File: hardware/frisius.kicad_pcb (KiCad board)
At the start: 4 copper layers, 50 x 50 mm, 93 parts, among them J1 MEM2067, J2 USB_C_Receptacle_USB2.0, J3 BATTERY, J4 Display, Q1 Q_Dual_NMOS_G1S2G2D2S1D1, SW1 RESET, SW2 BOOT, SW3 POWER, U2 FXOS8700CQR1, U3 MS5637-02BA03, U4 L96-M33, U6 ESP32-S3-WROOM-1, U7 TLV62569DBV, U8 MP2723, U9 MAX17048G

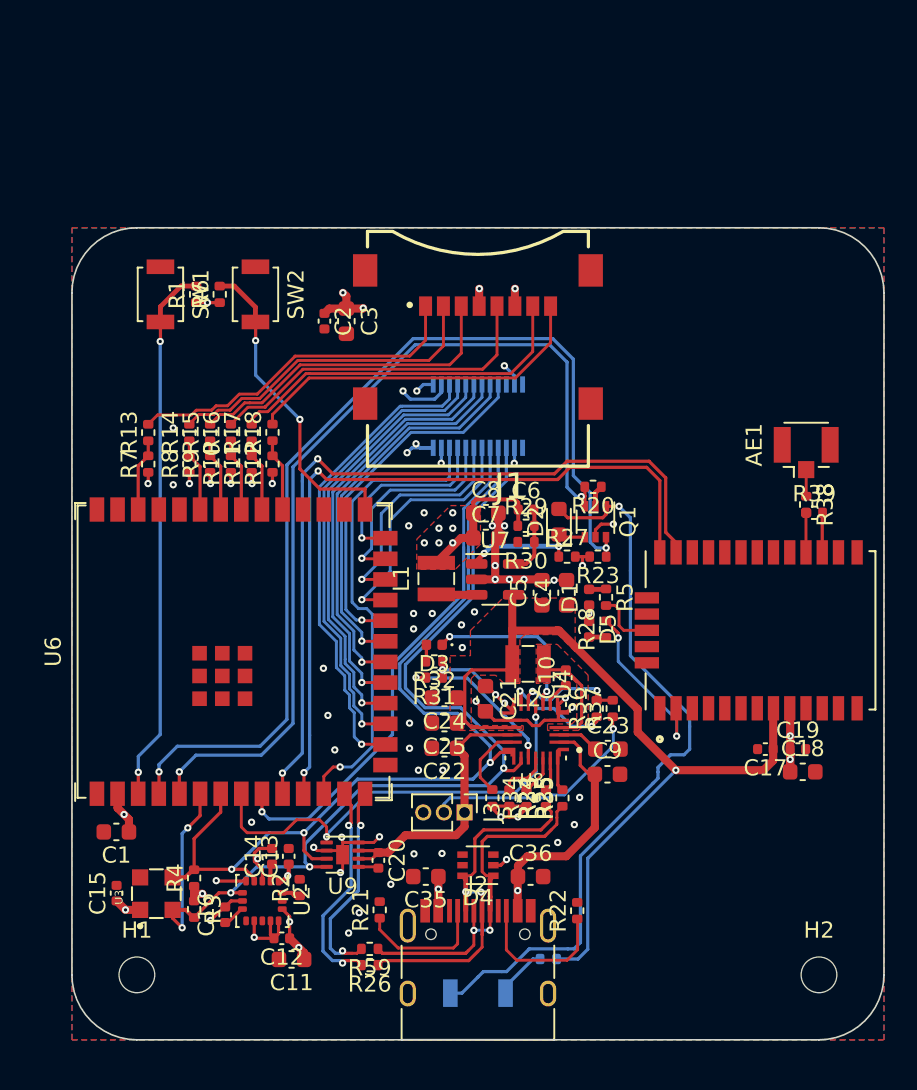
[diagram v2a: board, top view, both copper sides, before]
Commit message: merged in lcdboard test work
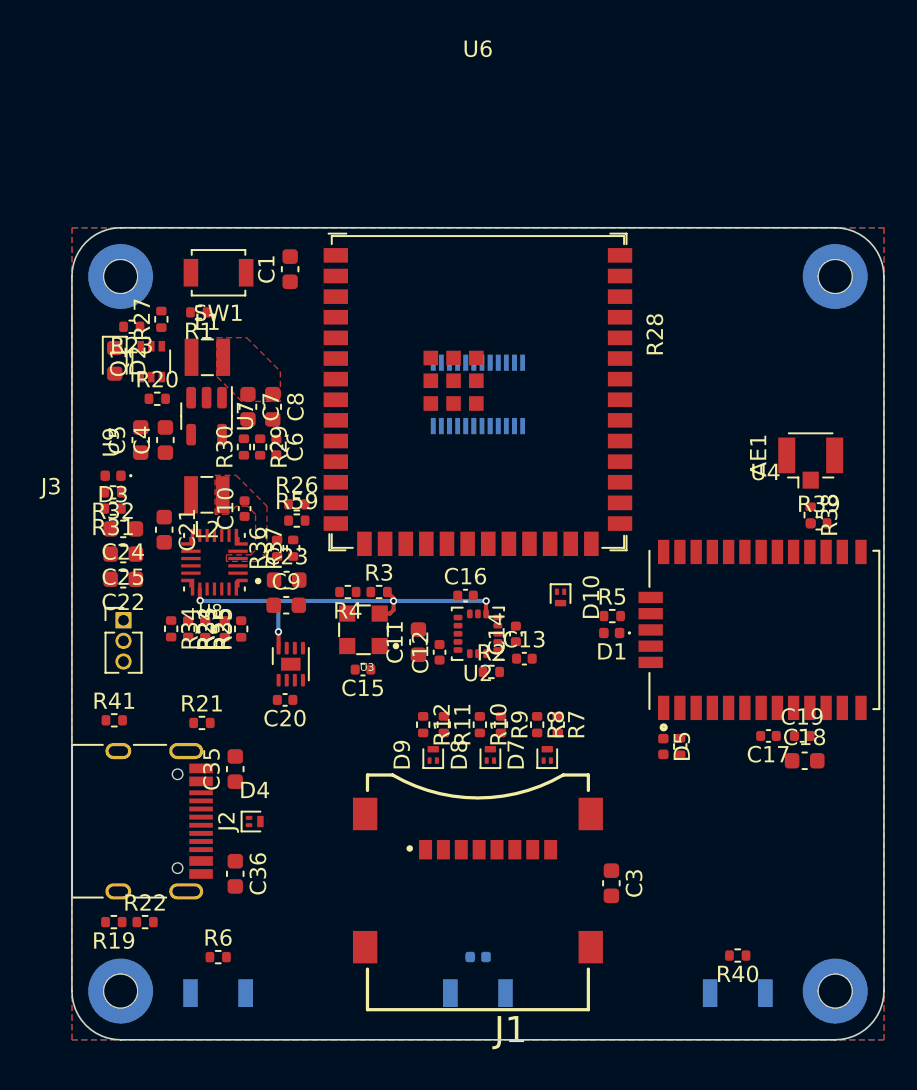
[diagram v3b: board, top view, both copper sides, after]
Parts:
- removed C2: 0.1u, Capacitor_SMD:C_0402_1005Metric
- removed R13, R14, R15, R16, R17, R18: 22, Resistor_SMD:R_0402_1005Metric
- added D10: PESD3V3L2UM, Package_TO_SOT_SMD:SOT-883, F.Cu at (76.7, 106.2)
- added D6: LED_Small_Filled, LED_SMD:LED_0402_1005Metric, B.Cu at (71.6, 128.3)
- added D7: PESD3V3L2UM, Package_TO_SOT_SMD:SOT-883, F.Cu at (75.8, 115.9)
- added D8: PESD3V3L2UM, Package_TO_SOT_SMD:SOT-883, F.Cu at (72.3, 115.9)
- added D9: PESD3V3L2UM, Package_TO_SOT_SMD:SOT-883, F.Cu at (68.8, 115.9)
- added H3: TL, Mounting_Wuerth:Mounting_Wuerth_WA-SMSI-M1.6_H2mm_9774020633, B.Cu at (93.6, 86.5)
- added H4: TR, Mounting_Wuerth:Mounting_Wuerth_WA-SMSI-M1.6_H2mm_9774020633, B.Cu at (49.6, 86.5)
- added R40: R_Small, Resistor_SMD:R_0402_1005Metric, F.Cu at (87.6, 128.3)
- added R41: 1k, Resistor_SMD:R_0402_1005Metric, F.Cu at (49.2, 113.8)
- added SW4: NAV, Button_Switch_SMD:SW_SPST_B3U-1000P, B.Cu at (55.6, 130.6)
- D4: value ESD5V5U5ULCE6327HTSA1 -> PESD3V3L2UM; footprint Package_TO_SOT_SMD:SOT-363_SC-70-6 -> Package_TO_SOT_SMD:SOT-883
- H1, H2: footprint MountingHole:MountingHole_2.2mm_M2_ISO7380 -> Mounting_Wuerth:Mounting_Wuerth_WA-SMSI-M1.6_H2mm_9774020633; moved to B.Cu
- R19: moved to F.Cu
- SW2: moved to B.Cu
- moved SW2 52.3 mm to (87.6, 130.6), turned to 180 degrees
- moved H1 43.0 mm to (93.6, 130.4), turned to 180 degrees
- moved H2 43.0 mm to (49.6, 130.4), turned to 180 degrees
- moved R6 40.8 mm to (55.6, 128.4), turned to 0 degrees
- moved C3 38.3 mm to (79.8, 123.8)
- moved C1 36.3 mm to (60.0, 86.0), turned to 90 degrees
- moved J1 33.5 mm to (71.6, 124.4)
- moved R23 32.0 mm to (50.2, 89.5)
- moved R7 29.9 mm to (76.5, 114.0), turned to -90 degrees
- moved D2 29.1 mm to (49.2, 91.6), turned to -90 degrees
- moved Q1 29.1 mm to (51.5, 91.7), turned to 90 degrees
- moved R27 28.9 mm to (52.1, 89.1), turned to 90 degrees
- moved R26 28.7 mm to (60.4, 100.5), turned to 0 degrees
- moved R20 27.4 mm to (51.8, 94.0), turned to 0 degrees
- moved R19 26.9 mm to (49.1, 126.2), turned to 180 degrees
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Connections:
- D4 pad 2: GND -> /Power/PORT_D-
- D4 pad 3: unconnected-(D4-Pad3) -> GND
- J1 pad 1: Net-(J1-Pad1) -> /Processor/SDMMC.D2
- J1 pad 2: Net-(J1-Pad2) -> /Processor/SDMMC.D3
- J1 pad 3: Net-(J1-Pad3) -> /Processor/SDMMC.CMD
- J1 pad 5: Net-(J1-Pad5) -> /Processor/SDMMC.CLK
- J1 pad 7: Net-(J1-Pad7) -> /Processor/SDMMC.D0
- J1 pad 8: Net-(J1-Pad8) -> /Processor/SDMMC.D1
- J4 pad 10: /Display/TOUCH_INT -> /Display/SYS_I2C.SCL
- J4 pad 12: /Display/MUXLINE0 -> /Display/LCD_SPI_CTRL
- J4 pad 14: /Display/MUXLINE1 -> /Display/MUXLINE3
- J4 pad 18: /Display/MUXLINE3 -> /Display/MUXLINE1
- J4 pad 20: /Display/LCD_SPI_CTRL -> /Display/MUXLINE0
- J4 pad 6: /Display/SYS_I2C.SDA -> /Display/TOUCH_INT
- J4 pad 8: /Display/SYS_I2C.SCL -> /Display/SYS_I2C.SDA
- R10 pad 2: /Processor/SDMMC.CLK -> /Processor/SDMMC.CMD
- R11 pad 2: /Processor/SDMMC.D0 -> /Processor/SDMMC.D3
- R12 pad 2: /Processor/SDMMC.D1 -> /Processor/SDMMC.D2
- R7 pad 2: /Processor/SDMMC.D2 -> /Processor/SDMMC.D1
- R8 pad 2: /Processor/SDMMC.D3 -> /Processor/SDMMC.D0
- R9 pad 2: /Processor/SDMMC.CMD -> /Processor/SDMMC.CLK
- U6 pad 10: /GPS/GPS_UART.RX -> unconnected-(U6-Pad10)
- U6 pad 11: /GPS/GPS_UART.TX -> unconnected-(U6-Pad11)
- U6 pad 12: /Display/LCD_SPI_CTRL -> unconnected-(U6-Pad12)
- U6 pad 15: /Processor/STATUS_LED -> Net-(R41-Pad2)
- U6 pad 16: /Display/DISPLAY_BL -> unconnected-(U6-Pad16)
- U6 pad 17: /Display/RGB.R0 -> /Display/MUXLINE0
- U6 pad 18: /Display/RGB.R1 -> /Display/MUXLINE1
- U6 pad 19: /Display/RGB.G0 -> /Display/MUXLINE2
- U6 pad 20: /Display/RGB.G1 -> /Display/MUXLINE3
- U6 pad 21: /Display/RGB.B0 -> /Display/LCD_SPI_CTRL
- U6 pad 22: /Display/RGB.B1 -> /Power/POWER_BUTTON
- U6 pad 23: /Display/MUXLINE0 -> /Power/SHUTDOWN
- U6 pad 24: /Display/MUXLINE1 -> /Display/SYS_I2C.SCL
- U6 pad 25: /Display/MUXLINE2 -> /Display/SYS_I2C.SDA
- U6 pad 26: /Display/MUXLINE3 -> /Display/TOUCH_INT
- U6 pad 31: /Processor/SDMMC.D1 -> /Display/RGB.B1
- U6 pad 32: /Processor/SDMMC.D0 -> /Display/RGB.B0
- U6 pad 33: /Processor/SDMMC.CLK -> /Display/RGB.G1
- U6 pad 34: /Processor/SDMMC.CMD -> /Display/RGB.G0
- U6 pad 35: /Processor/SDMMC.D3 -> /Display/RGB.R1
- U6 pad 38: /Processor/SDMMC.D2 -> /Display/RGB.R0
- U6 pad 4: /Power/POWER_BUTTON -> unconnected-(U6-Pad4)
- U6 pad 5: /Power/SHUTDOWN -> unconnected-(U6-Pad5)
- U6 pad 6: /Display/SYS_I2C.SDA -> unconnected-(U6-Pad6)
- U6 pad 7: /Display/SYS_I2C.SCL -> unconnected-(U6-Pad7)
- U6 pad 8: /Power/BMS_INT -> unconnected-(U6-Pad8)
- U6 pad 9: /Display/TOUCH_INT -> unconnected-(U6-Pad9)
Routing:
- net /Power/POWER_BUTTON: track 61.9 -> 0.00 mm, vias 2 -> 0
- net /Display/SYS_I2C.SCL: track 59.4 -> 0.00 mm, vias 3 -> 0
- net /Power/SHUTDOWN: track 56.1 -> 0.00 mm, vias 2 -> 0
- net GND: track 53.6 -> 0.00 mm, vias 53 -> 0
- net VDD_NVDC: track 52.7 -> 0.00 mm, vias 1 -> 0
- net /GPS/GPS_UART.RX: track 48.9 -> 0.00 mm, vias 2 -> 0
- net /GPS/GPS_UART.TX: track 46.6 -> 0.00 mm, vias 2 -> 0
- net Net-(D2-Pad2): track 45.7 -> 0.00 mm, vias 1 -> 0
- net +3V3: track 44.5 -> 0.00 mm, vias 29 -> 0
- net /Display/SYS_I2C.SDA: track 65.2 -> 24.3 mm, vias 5 -> 4
- net /Processor/RST_BTN: track 33.3 -> 0.00 mm, vias 2 -> 0
- net /Display/TOUCH_INT: track 31.6 -> 0.00 mm, vias 1 -> 0
- net /Display/DISPLAY_BL: track 29.5 -> 0.00 mm, vias 1 -> 0
- net /Display/LCD_SPI_CTRL: track 29.1 -> 0.00 mm, vias 1 -> 0
- net /Display/RGB.R0: track 28.3 -> 0.00 mm, vias 1 -> 0
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- removed copper zone on F.Cu, net VDD_NVDC
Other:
- outline, holes or cut-outs redrawn
- rule pad_to_mask_clearance: 0.05 -> 0
- board text removed: "CORE"
